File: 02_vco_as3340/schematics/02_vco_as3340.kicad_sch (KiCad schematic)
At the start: 89 parts, among them J1 Eurorack 10 pin header, J10 Triangle Out, J11 Sine Out, J2 1V/O IN, J3 Positive Hard Sync IN, J4 Negative Hard Sync IN, J5 Soft Sync In, J6 FM IN, J7 PWM CV IN, J8 Square Out, J9 Sawtooth Out, Q1 2N3904, Q2 2N3904, SW1 SW_SPDT, U1 TL074, U2 AS3340, U3 TL072

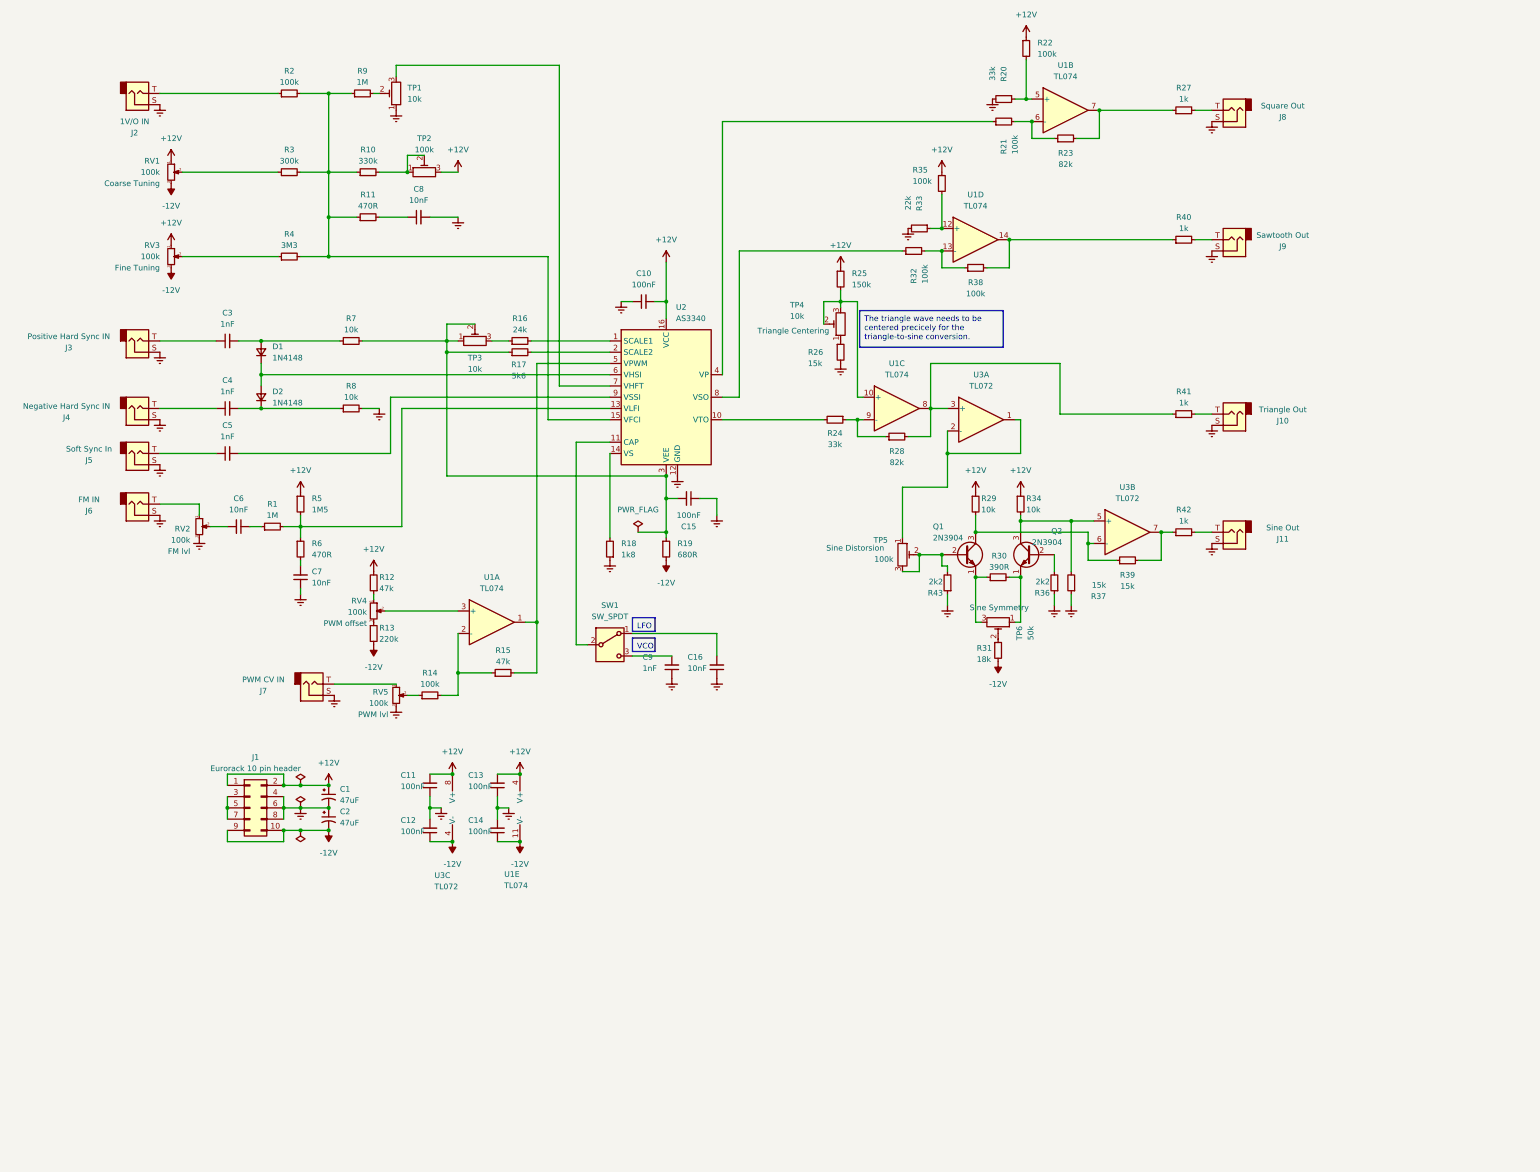
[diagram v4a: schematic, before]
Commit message: added PCB for 02
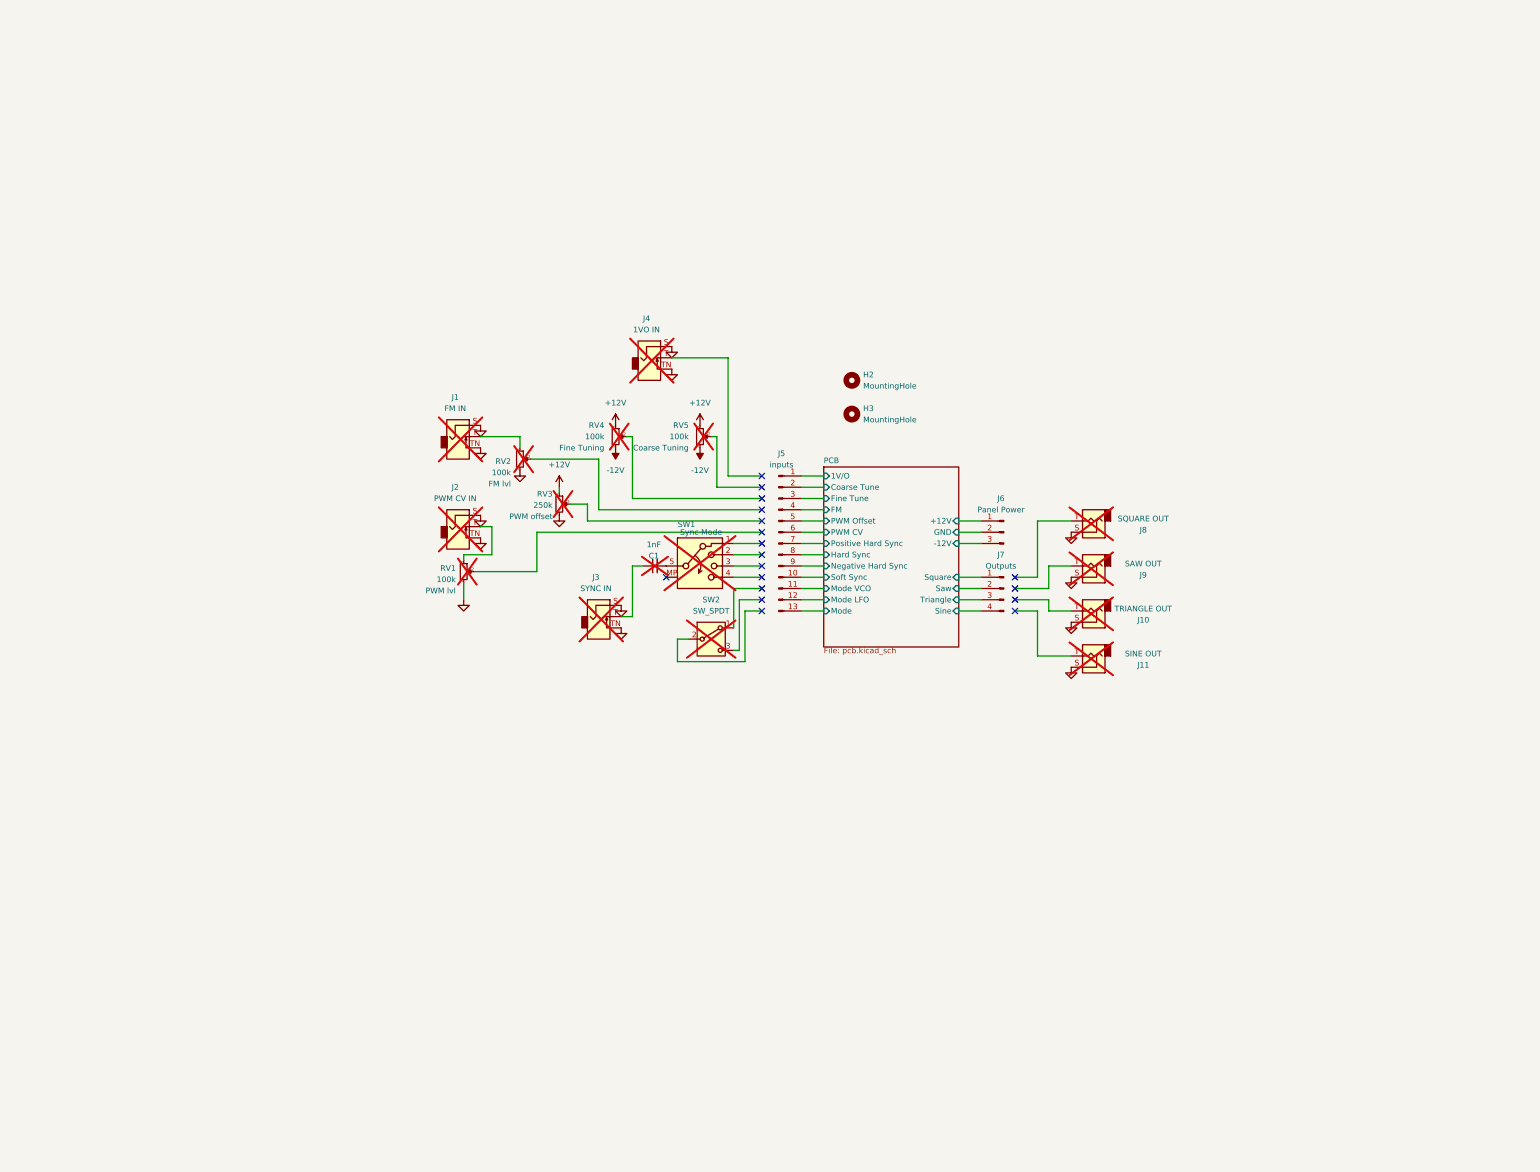
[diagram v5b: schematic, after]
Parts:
- removed C1, C2: 47uF, Capacitor_THT:CP_Radial_D6.3mm_P2.50mm, symbol Device:C_Polarized_Small_US
- removed C10, C11, C12, C13, C14, C15: 100nF, Capacitor_THT:C_Disc_D6.0mm_W2.5mm_P5.00mm, symbol Device:C_Small
- removed C16, C6, C7, C8: 10nF, Capacitor_THT:C_Disc_D6.0mm_W2.5mm_P5.00mm, symbol Device:C_Small
- removed C3, C4, C5, C9: 1nF, Capacitor_THT:C_Disc_D6.0mm_W2.5mm_P5.00mm, symbol Device:C_Small
- removed D1, D2: 1N4148, Diode_THT:D_A-405_P10.16mm_Horizontal, symbol Device:D_Small
- removed J1: Eurorack 10 pin header, Connector_PinHeader_2.54mm:PinHeader_2x05_P2.54mm_Vertical, symbol Connector_Generic:Conn_02x05_Odd_Even
- removed J2: 1V/O IN, Connector_Audio:Jack_6.35mm_Neutrik_NJ5FD-V_Vertical, symbol Connector_Audio:AudioJack2
- removed J3: Positive Hard Sync IN, Connector_Audio:Jack_6.35mm_Neutrik_NJ5FD-V_Vertical, symbol Connector_Audio:AudioJack2
- removed J4: Negative Hard Sync IN, Connector_Audio:Jack_6.35mm_Neutrik_NJ5FD-V_Vertical, symbol Connector_Audio:AudioJack2
- removed J5: Soft Sync In, Connector_Audio:Jack_6.35mm_Neutrik_NJ5FD-V_Vertical, symbol Connector_Audio:AudioJack2
- removed J6: FM IN, Connector_Audio:Jack_6.35mm_Neutrik_NJ5FD-V_Vertical, symbol Connector_Audio:AudioJack2
- removed J7: PWM CV IN, Connector_Audio:Jack_6.35mm_Neutrik_NJ5FD-V_Vertical, symbol Connector_Audio:AudioJack2
- removed Q1, Q2: 2N3904, Package_TO_SOT_THT:TO-92_Inline, symbol Transistor_BJT:2N3904
- removed R1, R9: 1M, Resistor_THT:R_Axial_DIN0207_L6.3mm_D2.5mm_P10.16mm_Horizontal, symbol Device:R_Small
- removed R10: 330k, Resistor_THT:R_Axial_DIN0207_L6.3mm_D2.5mm_P10.16mm_Horizontal, symbol Device:R_Small
- removed R11, R6: 470R, Resistor_THT:R_Axial_DIN0207_L6.3mm_D2.5mm_P10.16mm_Horizontal, symbol Device:R_Small
- removed R12, R15: 47k, Resistor_THT:R_Axial_DIN0207_L6.3mm_D2.5mm_P10.16mm_Horizontal, symbol Device:R_Small
- removed R13: 220k, Resistor_THT:R_Axial_DIN0207_L6.3mm_D2.5mm_P10.16mm_Horizontal, symbol Device:R_Small
- removed R14, R2, R21, R22, R32, R35, R38: 100k, Resistor_THT:R_Axial_DIN0207_L6.3mm_D2.5mm_P10.16mm_Horizontal, symbol Device:R_Small
- removed R16: 24k, Resistor_THT:R_Axial_DIN0207_L6.3mm_D2.5mm_P10.16mm_Horizontal, symbol Device:R_Small
- removed R17: 5k6, Resistor_THT:R_Axial_DIN0207_L6.3mm_D2.5mm_P10.16mm_Horizontal, symbol Device:R_Small
- removed R18: 1k8, Resistor_THT:R_Axial_DIN0207_L6.3mm_D2.5mm_P10.16mm_Horizontal, symbol Device:R_Small
- removed R19: 680R, Resistor_THT:R_Axial_DIN0207_L6.3mm_D2.5mm_P10.16mm_Horizontal, symbol Device:R_Small
- removed R20, R24: 33k, Resistor_THT:R_Axial_DIN0207_L6.3mm_D2.5mm_P10.16mm_Horizontal, symbol Device:R_Small
- removed R23, R28: 82k, Resistor_THT:R_Axial_DIN0207_L6.3mm_D2.5mm_P10.16mm_Horizontal, symbol Device:R_Small
- removed R25: 150k, Resistor_THT:R_Axial_DIN0207_L6.3mm_D2.5mm_P10.16mm_Horizontal, symbol Device:R_Small
- removed R26, R37, R39: 15k, Resistor_THT:R_Axial_DIN0207_L6.3mm_D2.5mm_P10.16mm_Horizontal, symbol Device:R_Small
- removed R27, R40, R41, R42: 1k, Resistor_THT:R_Axial_DIN0207_L6.3mm_D2.5mm_P10.16mm_Horizontal, symbol Device:R_Small
- removed R29, R34, R7, R8: 10k, Resistor_THT:R_Axial_DIN0207_L6.3mm_D2.5mm_P10.16mm_Horizontal, symbol Device:R_Small
- removed R3: 300k, Resistor_THT:R_Axial_DIN0207_L6.3mm_D2.5mm_P10.16mm_Horizontal, symbol Device:R_Small
- removed R30: 390R, Resistor_THT:R_Axial_DIN0207_L6.3mm_D2.5mm_P10.16mm_Horizontal, symbol Device:R_Small
- removed R31: 18k, Resistor_THT:R_Axial_DIN0207_L6.3mm_D2.5mm_P10.16mm_Horizontal, symbol Device:R_Small
- removed R33: 22k, Resistor_THT:R_Axial_DIN0207_L6.3mm_D2.5mm_P10.16mm_Horizontal, symbol Device:R_Small
- removed R36, R43: 2k2, Resistor_THT:R_Axial_DIN0207_L6.3mm_D2.5mm_P10.16mm_Horizontal, symbol Device:R_Small
- removed R4: 3M3, Resistor_THT:R_Axial_DIN0207_L6.3mm_D2.5mm_P10.16mm_Horizontal, symbol Device:R_Small
- removed R5: 1M5, Resistor_THT:R_Axial_DIN0207_L6.3mm_D2.5mm_P10.16mm_Horizontal, symbol Device:R_Small
- removed SW1: SW_SPDT, symbol Switch:SW_SPDT
- removed TP1, TP3, TP4: 10k, Potentiometer_THT:Potentiometer_Vishay_T73XW_Horizontal, symbol Device:R_Potentiometer_Trim
- removed TP2, TP5: 100k, Potentiometer_THT:Potentiometer_Vishay_T73XW_Horizontal, symbol Device:R_Potentiometer_Trim
- removed TP6: 50k, Potentiometer_THT:Potentiometer_Vishay_T73XW_Horizontal, symbol Device:R_Potentiometer_Trim
- removed U1: TL074, Package_DIP:DIP-14_W10.16mm, symbol Amplifier_Operational:TL074
- removed U2: AS3340, Package_DIP:DIP-16_W7.62mm, symbol Audio:AS3340
- removed U3: TL072, Package_DIP:DIP-8_W10.16mm, symbol Amplifier_Operational:TL072
- added C1: 1nF, symbol Device:C_Small
- added H2, H3: MountingHole, MountingHole:MountingHole_3.2mm_M3_DIN965_Pad, symbol Mechanical:MountingHole
- added J1: FM IN, symbol Connector_Audio:AudioJack2_SwitchT
- added J2: PWM CV IN, symbol Connector_Audio:AudioJack2_SwitchT
- added J3: SYNC IN, symbol Connector_Audio:AudioJack2_SwitchT
- added J4: 1VO IN, symbol Connector_Audio:AudioJack2_SwitchT
- added J5: inputs, Connector_PinHeader_2.54mm:PinHeader_1x13_P2.54mm_Vertical, symbol Connector:Conn_01x13_Pin
- added J6: Panel Power, Connector_PinHeader_2.54mm:PinHeader_1x03_P2.54mm_Vertical, symbol Connector:Conn_01x03_Pin
- added J7: Outputs, Connector_PinHeader_2.54mm:PinHeader_1x04_P2.54mm_Vertical, symbol Connector:Conn_01x04_Pin
- added SW1: SW_Rotary_1x4, symbol Switch:SW_Rotary_1x4_MP
- added SW2: SW_SPDT, symbol Switch:SW_SPDT
- J10: value Triangle Out -> TRIANGLE OUT; footprint Connector_Audio:Jack_6.35mm_Neutrik_NJ5FD-V_Vertical -> (none); now not fitted
- J11: value Sine Out -> SINE OUT; footprint Connector_Audio:Jack_6.35mm_Neutrik_NJ5FD-V_Vertical -> (none); now not fitted
- J8: value Square Out -> SQUARE OUT; footprint Connector_Audio:Jack_6.35mm_Neutrik_NJ5FD-V_Vertical -> (none); now not fitted
- J9: value Sawtooth Out -> SAW OUT; footprint Connector_Audio:Jack_6.35mm_Neutrik_NJ5FD-V_Vertical -> (none); now not fitted
- RV1, RV2, RV4, RV5: footprint Potentiometer_THT:Potentiometer_Alpha_RD901F-40-00D_Single_Vertical_CircularHoles -> (none); now not fitted
- RV3: value 100k -> 250k; footprint Potentiometer_THT:Potentiometer_Alpha_RD901F-40-00D_Single_Vertical_CircularHoles -> (none); now not fitted
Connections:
- net +12V: now also RV4.1, RV5.1; no longer RV1.1
- net -12V: now also RV4.3, RV5.3; no longer RV1.3, RV3.3
- net at RV2.1: now also J1.T
- net GNDREF renamed GND
- net GND: now also RV1.3, RV3.3, J1.S, J1.TN, J2.S, J2.TN, J3.S, J3.TN, J4.S, J4.TN; no longer RV5.3
- new net: J2.T, RV1.1
- new net: C1.1, J3.T
- new net: C1.2, SW1.5
- new net PCB/+12V: J6.1 (Pin_1)
- new net PCB/-12V: J6.3 (Pin_3)
- new net PCB/1V/O: J5.1 (Pin_1)
- new net PCB/Coarse Tune: J5.2 (Pin_2)
- new net PCB/FM: J5.4 (Pin_4)
- new net PCB/Fine Tune: J5.3 (Pin_3)
- new net PCB/GND: J6.2 (Pin_2)
- new net PCB/Hard Sync: J5.8 (Pin_8)
- new net PCB/Mode: J5.13 (Pin_13)
- new net PCB/Mode LFO: J5.12 (Pin_12)
- new net PCB/Mode VCO: J5.11 (Pin_11)
- new net PCB/Negative Hard Sync: J5.9 (Pin_9)
- new net PCB/PWM CV: J5.6 (Pin_6)
- new net PCB/PWM Offset: J5.5 (Pin_5)
- new net PCB/Positive Hard Sync: J5.7 (Pin_7)
- new net PCB/Saw: J7.2 (Pin_2)
- new net PCB/Sine: J7.4 (Pin_4)
- new net PCB/Soft Sync: J5.10 (Pin_10)
- new net PCB/Square: J7.1 (Pin_1)
- new net PCB/Triangle: J7.3 (Pin_3)
- no-connect marks 0 -> 18
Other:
- added sheet PCB (pcb.kicad_sch)

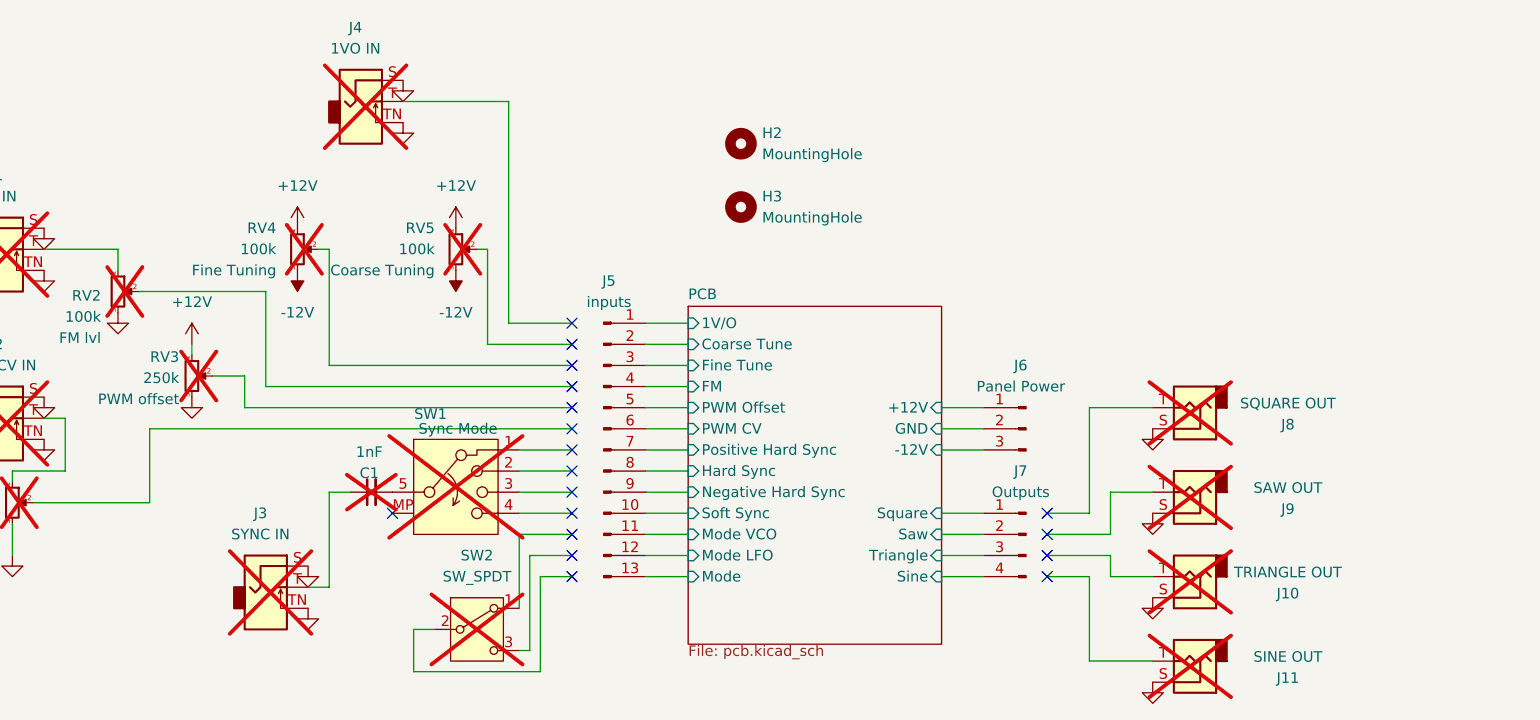
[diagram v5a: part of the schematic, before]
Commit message: updated PCBs for 02 and 03
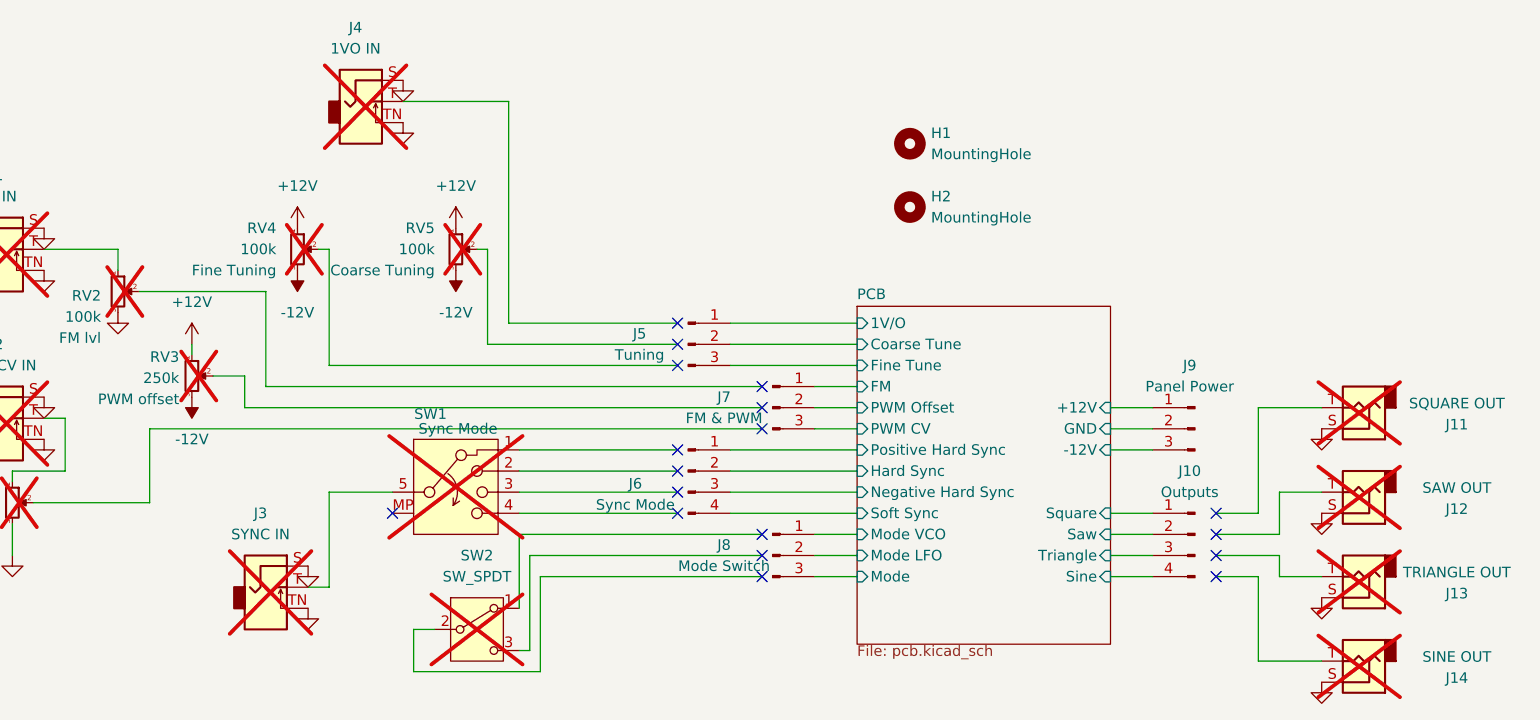
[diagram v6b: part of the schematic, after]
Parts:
- removed C1: 1nF, symbol Device:C_Small
- removed J5: inputs, Connector_PinHeader_2.54mm:PinHeader_1x13_P2.54mm_Vertical, symbol Connector:Conn_01x13_Pin
- added J5: Tuning, Connector_PinHeader_2.54mm:PinHeader_1x03_P2.54mm_Vertical, symbol Connector:Conn_01x03_Pin
- added J6: Sync Mode, Connector_PinHeader_2.54mm:PinHeader_1x04_P2.54mm_Vertical, symbol Connector:Conn_01x04_Pin
- added J7: FM & PWM, Connector_PinHeader_2.54mm:PinHeader_1x03_P2.54mm_Vertical, symbol Connector:Conn_01x03_Pin
- added J8: Mode Switch, Connector_PinHeader_2.54mm:PinHeader_1x03_P2.54mm_Vertical, symbol Connector:Conn_01x03_Pin
- H1: renamed from H2; footprint MountingHole:MountingHole_3.2mm_M3_DIN965_Pad -> MountingHole:MountingHole_3.2mm_M3
- H2: renamed from H3; footprint MountingHole:MountingHole_3.2mm_M3_DIN965_Pad -> MountingHole:MountingHole_3.2mm_M3
- renumbered J7 to J10, J8 to J11, J9 to J12, J10 to J13, J11 to J14, J6 to J9
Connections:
- net -12V: now also RV3.3
- net GND: no longer RV3.3
- net PCB/1V/O: now also J5.1 (Pin_1)
- net PCB/Coarse Tune: now also J5.2 (Pin_2)
- net PCB/FM: now also J7.1 (Pin_1)
- net PCB/Fine Tune: now also J5.3 (Pin_3)
- net PCB/Hard Sync: now also J6.2 (Pin_2)
- net PCB/Mode: now also J8.3 (Pin_3)
- net PCB/Mode LFO: now also J8.2 (Pin_2)
- net PCB/Mode VCO: now also J8.1 (Pin_1)
- net PCB/Negative Hard Sync: now also J6.3 (Pin_3)
- net PCB/PWM CV: now also J7.3 (Pin_3)
- net PCB/PWM Offset: now also J7.2 (Pin_2)
- net PCB/Positive Hard Sync: now also J6.1 (Pin_1)
- net PCB/Soft Sync: now also J6.4 (Pin_4)
- net at J3.T: now also SW1.5
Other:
- moved on the sheet: H1, H2, J10, J11, J12, J13, J14, J9
